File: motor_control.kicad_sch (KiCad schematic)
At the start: 4 parts, among them U3 DRV8870DDA

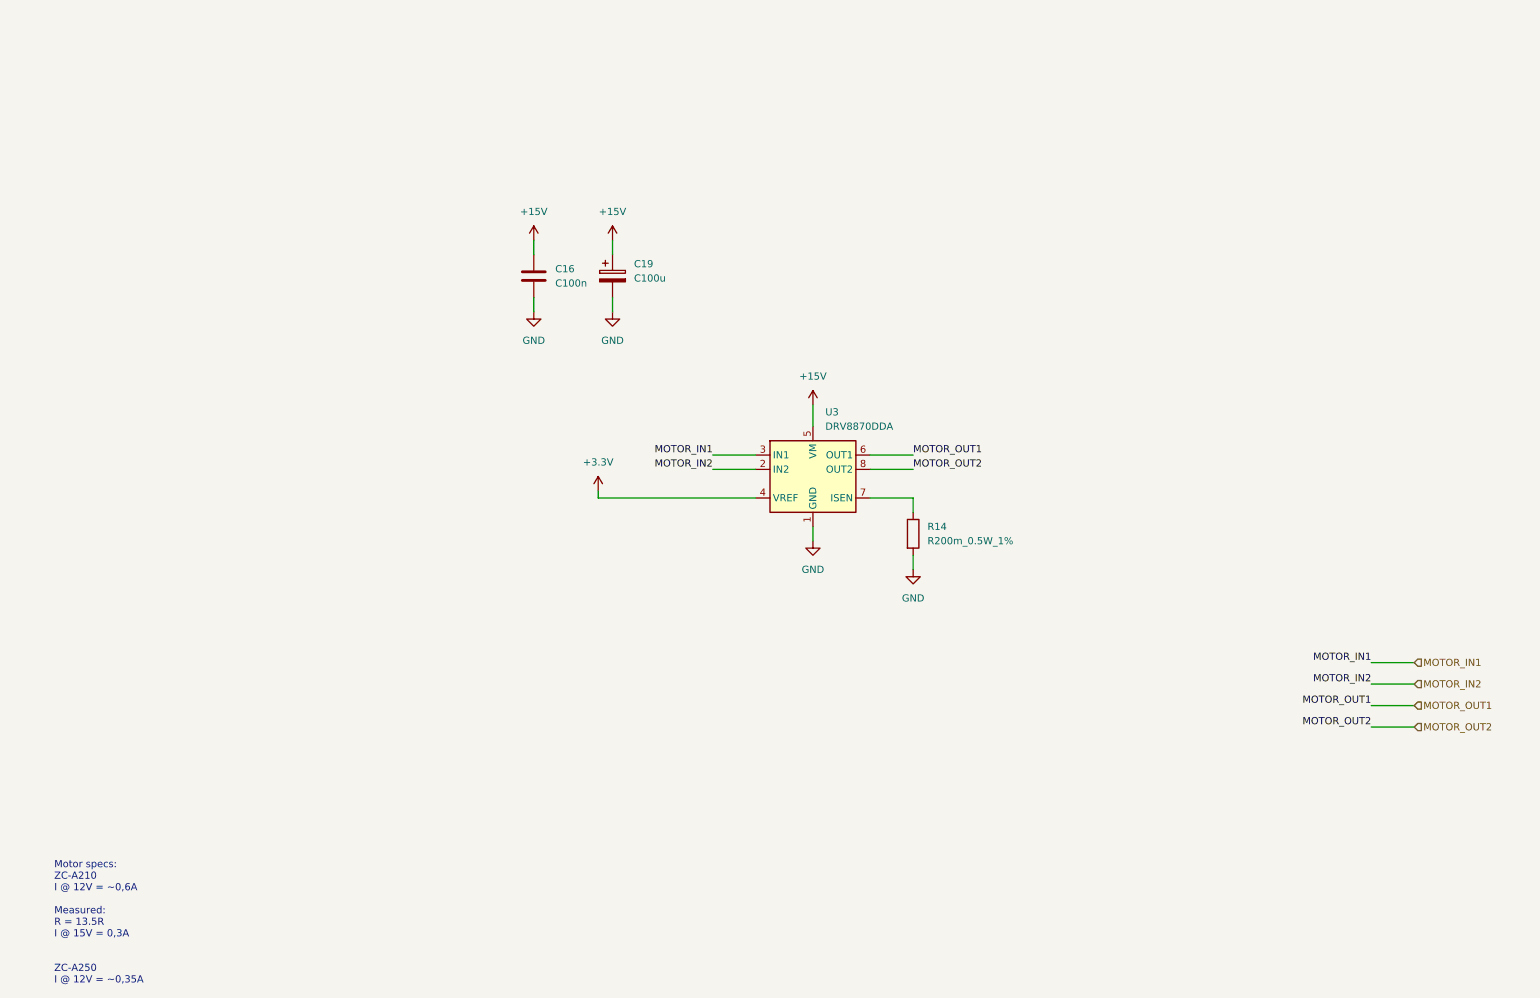
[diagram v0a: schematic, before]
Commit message: Add ESP32-S3-WROOM-1, 5V rail and UI sheet
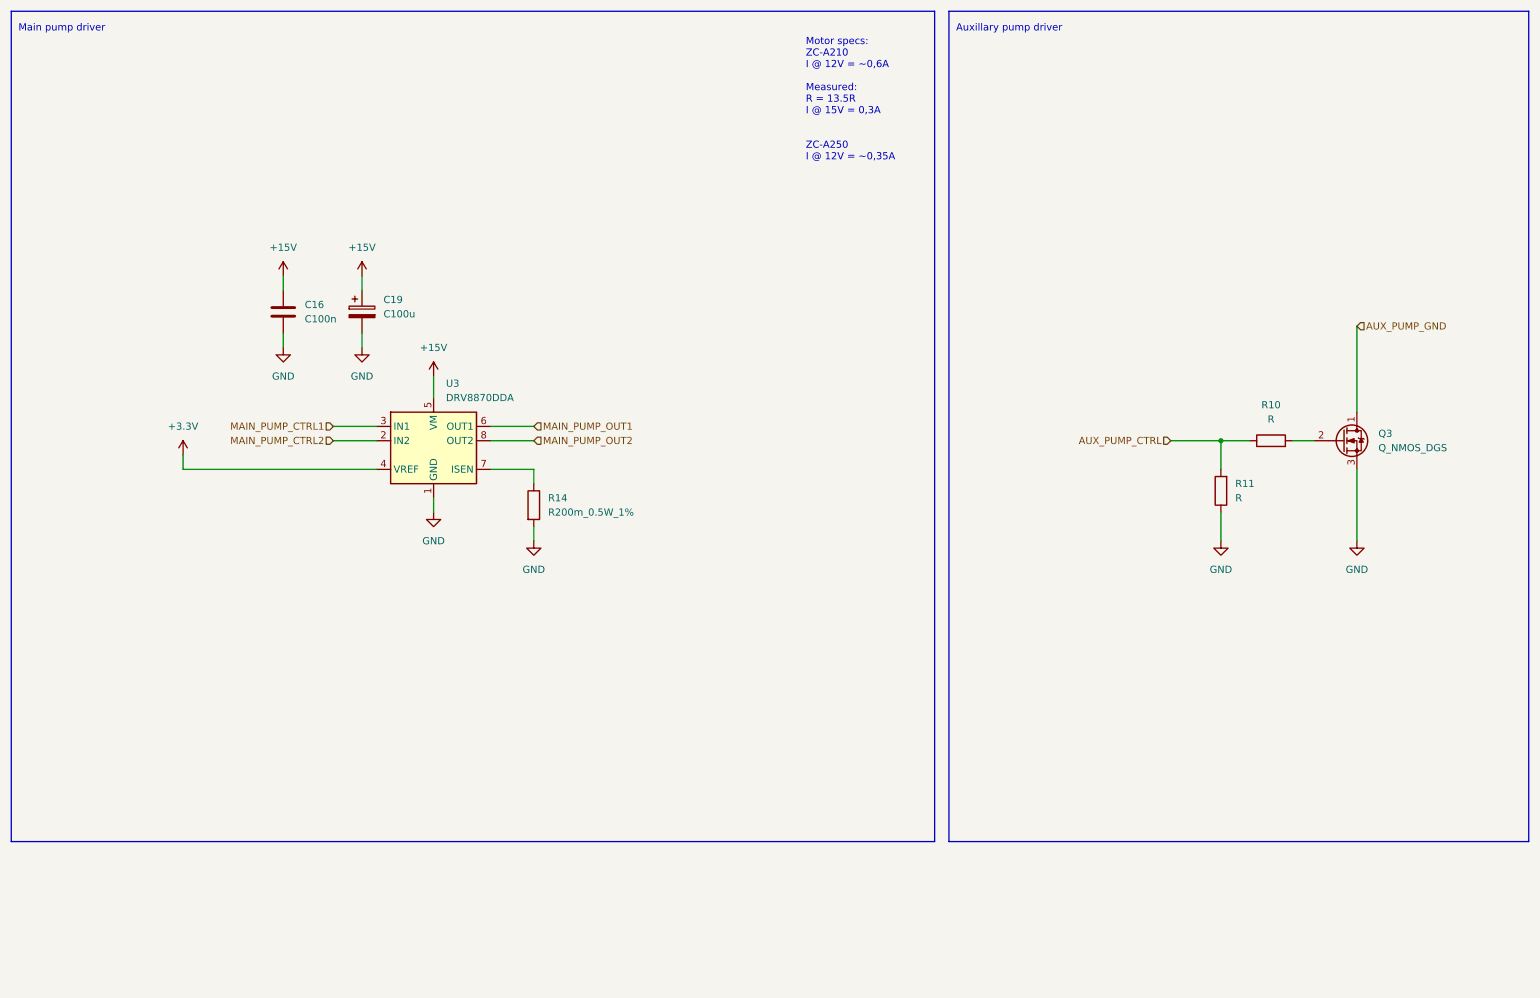
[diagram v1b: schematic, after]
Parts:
- added Q3: Q_NMOS_DGS, symbol Device:Q_NMOS_DGS
- added R10, R11: R, symbol Device:R
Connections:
- net GND: now also Q3.3 (S), R11.1
- net MOTOR_IN1 renamed MAIN_PUMP_CTRL1
- net MOTOR_IN2 renamed MAIN_PUMP_CTRL2
- net MOTOR_OUT1 renamed MAIN_PUMP_OUT1
- net MOTOR_OUT2 renamed MAIN_PUMP_OUT2
- new net: Q3.2 (G), R10.2
- new net AUX_PUMP_CTRL: R10.1, R11.2
- new net AUX_PUMP_GND: Q3.1 (D)
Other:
- note added: "Auxillary pump driver"
- note added: "Main pump driver"
- moved on the sheet: C16, C19, R14, U3

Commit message: Finish first design
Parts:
- removed Q3: Q_NMOS_DGS, symbol Device:Q_NMOS_DGS
- removed R11: R, symbol Device:R
- added D3: S1A-13-F, Diode_SMD:D_SMA, symbol Device:D
- added JP1: SolderJumper_3_Bridged12, Jumper:SolderJumper-3_P1.3mm_Bridged12_RoundedPad1.0x1.5mm_NumberLabels, symbol Jumper:SolderJumper_3_Bridged12
- added Q3: IRLML2502, Package_TO_SOT_SMD:SOT-23, symbol Device:Q_NMOS_GSD
- added R30: R100k, Resistor_SMD:R_0805_2012Metric, symbol Device:R
- C16: value C100n -> C100n_20V; footprint (none) -> Capacitor_SMD:C_0805_2012Metric; Mouser Part Number (none) -> 187-CL21B104KACNNNC
- C19: value C100u -> C100u_20V; footprint (none) -> Capacitor_SMD:CP_Elec_6.3x5.9; Mouser Part Number (none) -> 647-PCM1D101MCL1GS
- R10: value R -> R120; footprint (none) -> Resistor_SMD:R_0805_2012Metric; Mouser Part Number (none) -> 603-AC0805FR-07120RL
- R14: value R200m_0.5W_1% -> R200m_1%_0.5W; footprint (none) -> Resistor_SMD:R_1206_3216Metric; Mouser Part Number (none) -> 504-MFLA1206R2000FS
- U3: value DRV8870DDA -> DRV8870DDAR; Mouser Part Number (none) -> 595-DRV8870DDAR
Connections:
- net +15V: now also D3.1 (K)
- net AUX_PUMP_CTRL: now also JP1.3 (B); no longer R10.1
- net AUX_PUMP_GND: now also D3.2 (A), Q3.3 (D)
- net GND: now also Q3.2 (S), R30.2
- net AUX_PUMP_GATE: now reaches R10.2
- net AUX_PUMP_GATE: now also Q3.1 (G), R30.1
- new net AUX_PUMP_SIGNAL: JP1.2 (C), R10.1
- new net WATER_LEVEL_SENSOR: JP1.1 (A)
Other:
- moved on the sheet: C16, C19, R10, R14, U3

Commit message: Re-annotate parts by board
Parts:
- renumbered C16 to C2, C19 to C5, D3 to D8, Q3 to Q8, R30 to R19, R14 to R2, R10 to R3, U3 to U2
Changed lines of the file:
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@@
   (symbol (lib_id "Device:Q_NMOS_GSD") (at 219.075 90.805 0) (unit 1)
     (in_bom yes) (on_board yes) (dnp no) (fields_autoplaced)
-    (property "Reference" "Q3" (at 224.79 89.535 0)
+    (property "Reference" "Q8" (at 224.79 89.535 0)
       (effects (font (size 1.27 1.27)) (justify left))
     )
@@
       (project "mainboard"
         (path "/613f8c39-c37c-4981-8911-5138d36a7959/ecb72cc6-9992-49a0-afcf-3c2905614ae7"
-          (reference "Q3") (unit 1)
+          (reference "Q8") (unit 1)
         )
       )
@@
   (symbol (lib_id "Device:R") (at 190.5 99.06 90) (unit 1)
     (in_bom yes) (on_board yes) (dnp no) (fields_autoplaced)
-    (property "Reference" "R10" (at 190.5 92.71 90)
+    (property "Reference" "R3" (at 190.5 92.71 90)
       (effects (font (size 1.27 1.27)))
     )
@@
       (project "mainboard"
         (path "/613f8c39-c37c-4981-8911-5138d36a7959/ecb72cc6-9992-49a0-afcf-3c2905614ae7"
-          (reference "R10") (unit 1)
+          (reference "R3") (unit 1)
         )
       )
@@
   (symbol (lib_id "Driver_Motor:DRV8870DDA") (at 115.57 99.06 0) (unit 1)
     (in_bom yes) (on_board yes) (dnp no) (fields_autoplaced)
-    (property "Reference" "U3" (at 117.7641 88.9 0)
+    (property "Reference" "U2" (at 117.7641 88.9 0)
       (effects (font (size 1.27 1.27)) (justify left))
     )
@@
       (project "mainboard"
         (path "/613f8c39-c37c-4981-8911-5138d36a7959/ecb72cc6-9992-49a0-afcf-3c2905614ae7"
-          (reference "U3") (unit 1)
+          (reference "U2") (unit 1)
         )
       )
@@
   (symbol (lib_id "Device:C_Polarized") (at 102.87 76.2 0) (unit 1)
     (in_bom yes) (on_board yes) (dnp no) (fields_autoplaced)
-    (property "Reference" "C19" (at 106.68 74.041 0)
+    (property "Reference" "C5" (at 106.68 74.041 0)
       (effects (font (size 1.27 1.27)) (justify left))
     )
@@
       (project "mainboard"
         (path "/613f8c39-c37c-4981-8911-5138d36a7959/ecb72cc6-9992-49a0-afcf-3c2905614ae7"
-          (reference "C19") (unit 1)
+          (reference "C5") (unit 1)
         )
       )
@@
   (symbol (lib_id "Device:R") (at 133.35 110.49 0) (unit 1)
     (in_bom yes) (on_board yes) (dnp no) (fields_autoplaced)
-    (property "Reference" "R14" (at 135.89 109.22 0)
+    (property "Reference" "R2" (at 135.89 109.22 0)
       (effects (font (size 1.27 1.27)) (justify left))
     )
@@
       (project "mainboard"
         (path "/613f8c39-c37c-4981-8911-5138d36a7959/ecb72cc6-9992-49a0-afcf-3c2905614ae7"
-          (reference "R14") (unit 1)
+          (reference "R2") (unit 1)
         )
       )
@@
   (symbol (lib_id "Device:D") (at 221.615 75.565 270) (unit 1)
     (in_bom yes) (on_board yes) (dnp no)
-    (property "Reference" "D3" (at 224.155 74.295 90)
+    (property "Reference" "D8" (at 224.155 74.295 90)
       (effects (font (size 1.27 1.27)) (justify left))
     )
@@
       (project "mainboard"
         (path "/613f8c39-c37c-4981-8911-5138d36a7959/ecb72cc6-9992-49a0-afcf-3c2905614ae7"
-          (reference "D3") (unit 1)
+          (reference "D8") (unit 1)
         )
       )
@@
   (symbol (lib_id "Device:C") (at 88.9 76.2 0) (mirror y) (unit 1)
     (in_bom yes) (on_board yes) (dnp no)
-    (property "Reference" "C16" (at 85.09 74.93 0)
+    (property "Reference" "C2" (at 85.09 74.93 0)
       (effects (font (size 1.27 1.27)) (justify left))
     )
@@
       (project "mainboard"
         (path "/613f8c39-c37c-4981-8911-5138d36a7959/ecb72cc6-9992-49a0-afcf-3c2905614ae7"
-          (reference "C16") (unit 1)
+          (reference "C2") (unit 1)
         )
       )
@@
   (symbol (lib_id "Device:R") (at 210.185 108.585 0) (unit 1)
     (in_bom yes) (on_board yes) (dnp no) (fields_autoplaced)
-    (property "Reference" "R30" (at 212.725 107.315 0)
+    (property "Reference" "R19" (at 212.725 107.315 0)
       (effects (font (size 1.27 1.27)) (justify left))
     )
@@
       (project "mainboard"
         (path "/613f8c39-c37c-4981-8911-5138d36a7959/ecb72cc6-9992-49a0-afcf-3c2905614ae7"
-          (reference "R30") (unit 1)
-        )
-      )
+          (reference "R19") (unit 1)
+        )
+      )

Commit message: Redesign power rails to use barrel jack 12V input
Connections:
- net +15V renamed +12V
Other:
- note added: "Motor specs: ZC-A250 I_load @ 12V = 0,35A"
- note removed: "Motor specs: ZC-A210 I @ 12V = ~0,6A Measured: R = 13.5R I @ 15V = 0,3A ZC-A250 I @ 12V = ~0,35A"
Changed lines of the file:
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@@
   (junction (at 210.185 99.06) (diameter 0) (color 0 0 0 0)
   )
+  (junction (at 88.9 69.85) (diameter 0) (color 0 0 0 0)
+  )
+  (junction (at 88.9 82.55) (diameter 0) (color 0 0 0 0)
+  )
   (junction (at 221.615 81.915) (diameter 0) (color 0 0 0 0)
   )
@@
     (stroke (width 0) (type default))
   )
+  (wire (pts (xy 88.9 69.85) (xy 88.9 67.31))
+    (stroke (width 0) (type default))
+  )
   (wire (pts (xy 221.615 67.945) (xy 221.615 71.755))
     (stroke (width 0) (type default))
   )
+  (wire (pts (xy 88.9 82.55) (xy 88.9 84.455))
+    (stroke (width 0) (type default))
+  )
   (wire (pts (xy 226.06 81.915) (xy 221.615 81.915))
     (stroke (width 0) (type default))
   )
+  (wire (pts (xy 88.9 82.55) (xy 102.87 82.55))
+    (stroke (width 0) (type default))
+  )
   (wire (pts (xy 179.07 88.9) (xy 189.23 88.9))
     (stroke (width 0) (type default))
@@
   )
   (wire (pts (xy 210.185 115.57) (xy 210.185 112.395))
+    (stroke (width 0) (type default))
+  )
+  (wire (pts (xy 102.87 69.85) (xy 88.9 69.85))
     (stroke (width 0) (type default))
   )
@@
     (effects (font (size 1.27 1.27)) (justify left bottom))
   )
-  (text "Motor specs:\nZC-A210\nI @ 12V = ~0,6A\n\nMeasured:\nR = 13.5R\nI @ 15V = 0,3A\n\n\nZC-A250\nI @ 12V = ~0,35A\n"
-    (at 132.715 83.82 0)
+  (text "Motor specs:\nZC-A250\nI_load @ 12V = 0,35A\n" (at 126.365 71.12 0)
     (effects (font (size 1.27 1.27)) (justify left bottom))
   )
@@
     (effects (font (size 1.27 1.27)) (justify right))
   )
-  (symbol (lib_id "power:GND") (at 102.87 82.55 0) (unit 1)
-    (in_bom yes) (on_board yes) (dnp no) (fields_autoplaced)
-    (property "Reference" "#PWR039" (at 102.87 88.9 0)
-      (effects (font (size 1.27 1.27)) hide)
-    )
-    (property "Value" "GND" (at 102.87 87.63 0)
-      (effects (font (size 1.27 1.27)))
-    )
-    (property "Footprint" "" (at 102.87 82.55 0)
-      (effects (font (size 1.27 1.27)) hide)
-    )
-    (property "Datasheet" "" (at 102.87 82.55 0)
-      (effects (font (size 1.27 1.27)) hide)
-    )
-    (pin "1")
-    (instances
-      (project "mainboard"
-        (path "/613f8c39-c37c-4981-8911-5138d36a7959/ecb72cc6-9992-49a0-afcf-3c2905614ae7"
-          (reference "#PWR039") (unit 1)
+  (symbol (lib_id "power:+12V") (at 221.615 67.945 0) (unit 1)
+    (in_bom yes) (on_board yes) (dnp no) (fields_autoplaced)
+    (property "Reference" "#PWR029" (at 221.615 71.755 0)
+      (effects (font (size 1.27 1.27)) hide)
+    )
+    (property "Value" "+12V" (at 221.615 63.5 0)
+      (effects (font (size 1.27 1.27)))
+    )
+    (property "Footprint" "" (at 221.615 67.945 0)
+      (effects (font (size 1.27 1.27)) hide)
+    )
+    (property "Datasheet" "" (at 221.615 67.945 0)
+      (effects (font (size 1.27 1.27)) hide)
+    )
+    (pin "1")
+    (instances
+      (project "mainboard"
+        (path "/613f8c39-c37c-4981-8911-5138d36a7959/ecb72cc6-9992-49a0-afcf-3c2905614ae7"
+          (reference "#PWR029") (unit 1)
         )
       )
@@
         (path "/613f8c39-c37c-4981-8911-5138d36a7959/ecb72cc6-9992-49a0-afcf-3c2905614ae7"
           (reference "Q8") (unit 1)
+        )
+      )
+    )
+  )
+  (symbol (lib_id "power:+12V") (at 88.9 67.31 0) (unit 1)
+    (in_bom yes) (on_board yes) (dnp no) (fields_autoplaced)
+    (property "Reference" "#PWR015" (at 88.9 71.12 0)
+      (effects (font (size 1.27 1.27)) hide)
+    )
+    (property "Value" "+12V" (at 88.9 62.865 0)
+      (effects (font (size 1.27 1.27)))
+    )
+    (property "Footprint" "" (at 88.9 67.31 0)
+      (effects (font (size 1.27 1.27)) hide)
+    )
+    (property "Datasheet" "" (at 88.9 67.31 0)
+      (effects (font (size 1.27 1.27)) hide)
+    )
+    (pin "1")
+    (instances
+      (project "mainboard"
+        (path "/613f8c39-c37c-4981-8911-5138d36a7959/ecb72cc6-9992-49a0-afcf-3c2905614ae7"
+          (reference "#PWR015") (unit 1)
         )
       )
@@
     )
   )
-  (symbol (lib_id "power:+15V") (at 115.57 87.63 0) (unit 1)
-    (in_bom yes) (on_board yes) (dnp no) (fields_autoplaced)
-    (property "Reference" "#PWR033" (at 115.57 91.44 0)
-      (effects (font (size 1.27 1.27)) hide)
-    )
-    (property "Value" "+15V" (at 115.57 82.55 0)
-      (effects (font (size 1.27 1.27)))
-    )
-    (property "Footprint" "" (at 115.57 87.63 0)
-      (effects (font (size 1.27 1.27)) hide)
-    )
-    (property "Datasheet" "" (at 115.57 87.63 0)
-      (effects (font (size 1.27 1.27)) hide)
-    )
-    (pin "1")
-    (instances
-      (project "mainboard"
-        (path "/613f8c39-c37c-4981-8911-5138d36a7959/ecb72cc6-9992-49a0-afcf-3c2905614ae7"
-          (reference "#PWR033") (unit 1)
-        )
-      )
-    )
-  )
   (symbol (lib_id "Device:R") (at 190.5 99.06 90) (unit 1)
     (in_bom yes) (on_board yes) (dnp no) (fields_autoplaced)
@@
         (path "/613f8c39-c37c-4981-8911-5138d36a7959/ecb72cc6-9992-49a0-afcf-3c2905614ae7"
           (reference "R3") (unit 1)
-        )
-      )
-    )
-  )
-  (symbol (lib_id "power:+15V") (at 88.9 69.85 0) (unit 1)
-    (in_bom yes) (on_board yes) (dnp no) (fields_autoplaced)
-    (property "Reference" "#PWR031" (at 88.9 73.66 0)
-      (effects (font (size 1.27 1.27)) hide)
-    )
-    (property "Value" "+15V" (at 88.9 64.77 0)
-      (effects (font (size 1.27 1.27)))
-    )
-    (property "Footprint" "" (at 88.9 69.85 0)
-      (effects (font (size 1.27 1.27)) hide)
-    )
-    (property "Datasheet" "" (at 88.9 69.85 0)
-      (effects (font (size 1.27 1.27)) hide)
-    )
-    (pin "1")
-    (instances
-      (project "mainboard"
-        (path "/613f8c39-c37c-4981-8911-5138d36a7959/ecb72cc6-9992-49a0-afcf-3c2905614ae7"
-          (reference "#PWR031") (unit 1)
-        )
-      )
-    )
-  )
-  (symbol (lib_id "power:+15V") (at 102.87 69.85 0) (unit 1)
-    (in_bom yes) (on_board yes) (dnp no) (fields_autoplaced)
-    (property "Reference" "#PWR032" (at 102.87 73.66 0)
-      (effects (font (size 1.27 1.27)) hide)
-    )
-    (property "Value" "+15V" (at 102.87 64.77 0)
-      (effects (font (size 1.27 1.27)))
-    )
-    (property "Footprint" "" (at 102.87 69.85 0)
-      (effects (font (size 1.27 1.27)) hide)
-    )
-    (property "Datasheet" "" (at 102.87 69.85 0)
-      (effects (font (size 1.27 1.27)) hide)
-    )
-    (pin "1")
-    (instances
-      (project "mainboard"
-        (path "/613f8c39-c37c-4981-8911-5138d36a7959/ecb72cc6-9992-49a0-afcf-3c2905614ae7"
-          (reference "#PWR032") (unit 1)
         )
       )
@@
     )
   )
-  (symbol (lib_id "power:GND") (at 88.9 82.55 0) (unit 1)
-    (in_bom yes) (on_board yes) (dnp no) (fields_autoplaced)
-    (property "Reference" "#PWR038" (at 88.9 88.9 0)
-      (effects (font (size 1.27 1.27)) hide)
-    )
-    (property "Value" "GND" (at 88.9 87.63 0)
-      (effects (font (size 1.27 1.27)))
-    )
-    (property "Footprint" "" (at 88.9 82.55 0)
-      (effects (font (size 1.27 1.27)) hide)
-    )
-    (property "Datasheet" "" (at 88.9 82.55 0)
+  (symbol (lib_id "power:GND") (at 88.9 84.455 0) (unit 1)
+    (in_bom yes) (on_board yes) (dnp no) (fields_autoplaced)
+    (property "Reference" "#PWR038" (at 88.9 90.805 0)
+      (effects (font (size 1.27 1.27)) hide)
+    )
+    (property "Value" "GND" (at 88.9 89.535 0)
+      (effects (font (size 1.27 1.27)))
+    )
+    (property "Footprint" "" (at 88.9 84.455 0)
+      (effects (font (size 1.27 1.27)) hide)
+    )
+    (property "Datasheet" "" (at 88.9 84.455 0)
       (effects (font (size 1.27 1.27)) hide)
     )
@@
     )
   )
+  (symbol (lib_id "power:+12V") (at 115.57 87.63 0) (unit 1)
+    (in_bom yes) (on_board yes) (dnp no) (fields_autoplaced)
+    (property "Reference" "#PWR014" (at 115.57 91.44 0)
+      (effects (font (size 1.27 1.27)) hide)
+    )
+    (property "Value" "+12V" (at 115.57 83.185 0)
+      (effects (font (size 1.27 1.27)))
+    )
+    (property "Footprint" "" (at 115.57 87.63 0)
+      (effects (font (size 1.27 1.27)) hide)
+    )
+    (property "Datasheet" "" (at 115.57 87.63 0)
+      (effects (font (size 1.27 1.27)) hide)
+    )
+    (pin "1")
+    (instances
+      (project "mainboard"
+        (path "/613f8c39-c37c-4981-8911-5138d36a7959/ecb72cc6-9992-49a0-afcf-3c2905614ae7"
+          (reference "#PWR014") (unit 1)
+        )
+      )
+    )
+  )
   (symbol (lib_id "power:+3.3V") (at 71.12 101.6 0) (unit 1)
     (in_bom yes) (on_board yes) (dnp no) (fields_autoplaced)
@@
         )
       )
-    )
-  )
-  (symbol (lib_id "power:+15V") (at 221.615 67.945 0) (unit 1)
-    (in_bom yes) (on_board yes) (dnp no) (fields_autoplaced)
-    (property "Reference" "#PWR060" (at 221.615 71.755 0)
-      (effects (font (size 1.27 1.27)) hide)
-    )
-    (property "Value" "+15V" (at 221.615 62.865 0)
-      (effects (font (size 1.27 1.27)))
-    )
-    (property "Footprint" "" (at 221.615 67.945 0)
-      (effects (font (size 1.27 1.27)) hide)
-    )
-    (property "Datasheet" "" (at 221.615 67.945 0)
-      (effects (font (size 1.27 1.27)) hide)
-    )
-    (pin "1")
-    (instances
-      (project "mainboard"
-        (path "/613f8c39-c37c-4981-8911-5138d36a7959/ecb72cc6-9992-49a0-afcf-3c2905614ae7"
-          (reference "#PWR060") (unit 1)
-        )
-      )
